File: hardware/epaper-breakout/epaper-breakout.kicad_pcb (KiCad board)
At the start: 2 copper layers, 100 x 40.5 mm, 101 parts, among them J1 XF2M-3315-1A, J2 C10418, J3 Conn_02x05_Counter_Clockwise, J4 ED060SC4, J5 Conn_01x01_Male, J6 Conn_01x01_Male, J7 Conn_01x12, Q1 AO3401A, Q3 MMBT3904, Q4 MMBT3904, U1 MCP1700-3302E_SOT23, U11 TP4056, U12 CH340C, U2 PCA9555PW, U3 TPS651851RSLR, U4 XC6206PxxxMR, U5 ESP32-WROVER, U6 ED060XC5

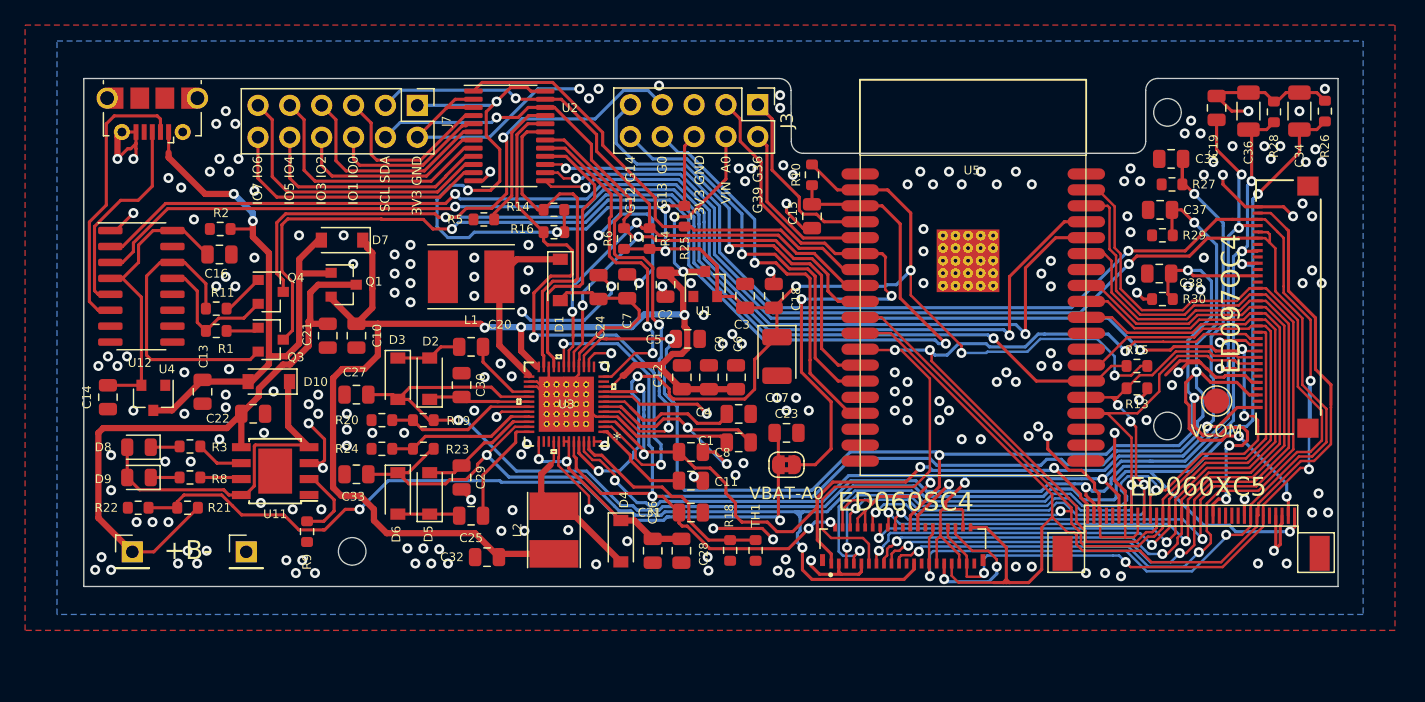
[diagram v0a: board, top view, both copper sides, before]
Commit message: add additional ground area
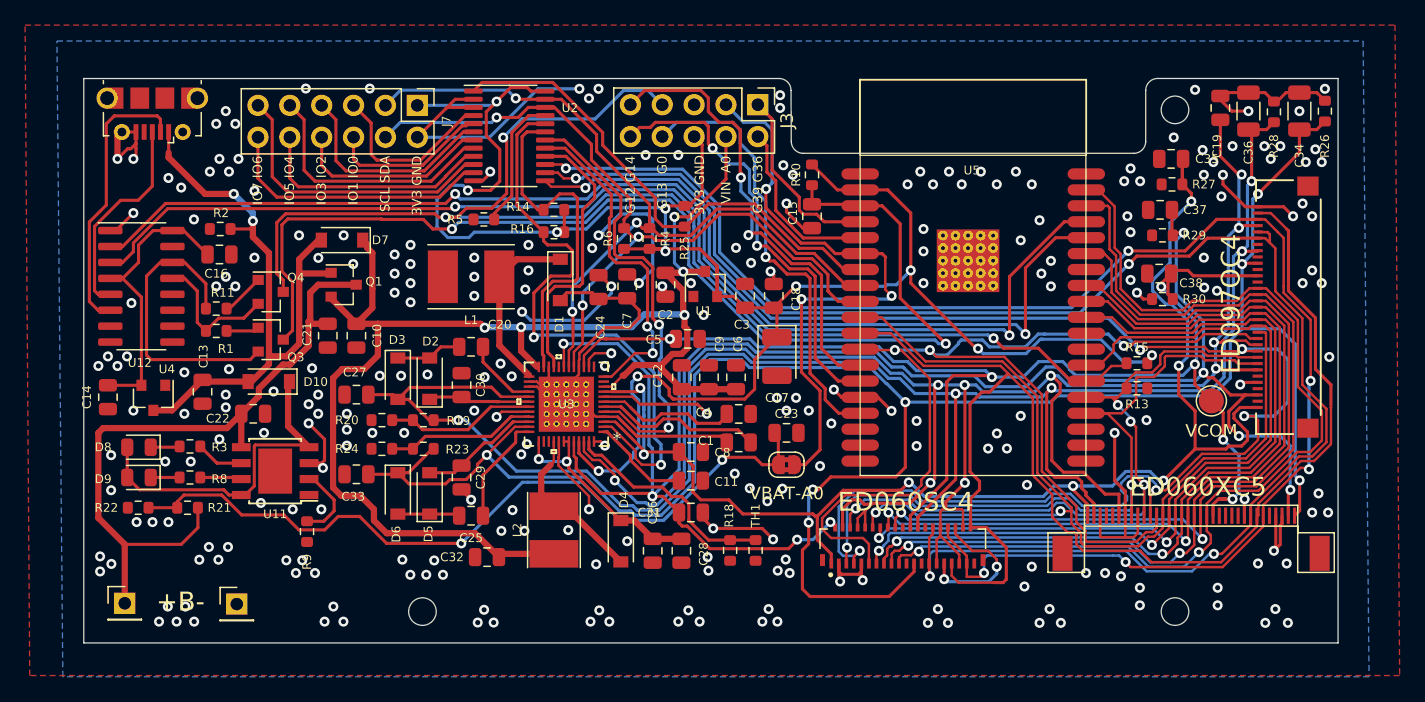
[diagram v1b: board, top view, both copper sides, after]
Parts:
- moved H3 14.8 mm to (112.0, 62.0)
- moved H2 7.38 mm to (52.0, 62.0)
- moved J6 4.23 mm to (37.2, 61.4)
- moved J5 4.14 mm to (28.3, 61.3)
- moved H1 0.63 mm to (112.0, 22.0)
- moved TP_VCOM1 0.42 mm to (114.9, 45.2)
- moved C19 0.30 mm to (115.6, 21.8)
- moved R15 0.22 mm to (109.0, 42.2)
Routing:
- net EPD_VDD: track 127.4 -> 155.2 mm, vias 8 -> 10
- net /+22V: track 147.0 -> 169.3 mm, vias 5 -> 7
- net /-20V: track 124.2 -> 144.9 mm
- net GND: track 198.8 -> 178.7 mm, vias 231 -> 261
- net /EP_VCOM: track 115.5 -> 104.3 mm
- net /EP_CKV: track 93.4 -> 102.9 mm
- net /EP_OE: track 122.5 -> 128.7 mm
- net BAT+: track 49.8 -> 54.9 mm
- net /EP_STV: track 131.1 -> 126.6 mm
- net /MOSI: track 31.4 -> 35.6 mm
- net /EP_D0: track 72.8 -> 76.3 mm
- net /MISO: track 32.1 -> 35.2 mm, vias 1 -> 2
- net /EP_STH: track 90.3 -> 92.8 mm
- net /SCL: track 61.3 -> 63.1 mm
- net /SDA: track 61.4 -> 63.1 mm
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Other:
- board size 100 x 40.5 mm -> 100 x 45 mm

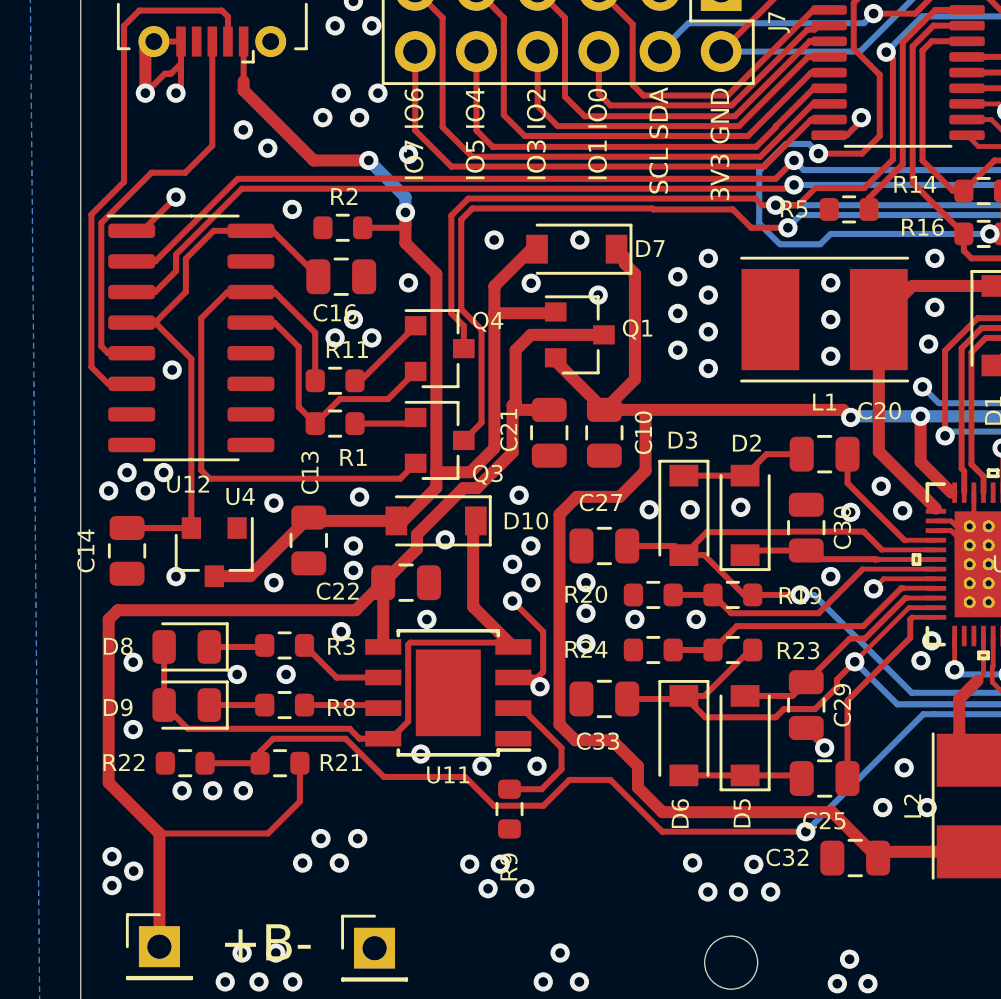
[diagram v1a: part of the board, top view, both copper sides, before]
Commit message: add tps2113 for power switchover
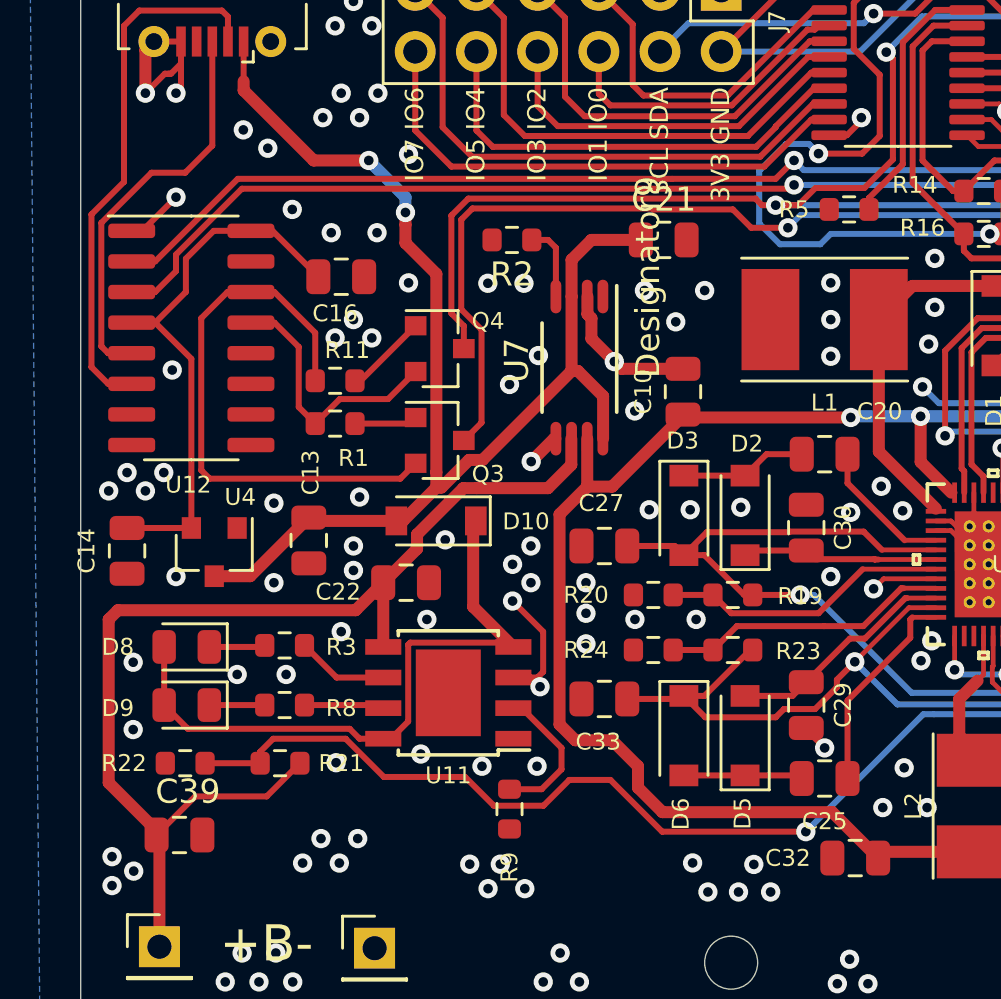
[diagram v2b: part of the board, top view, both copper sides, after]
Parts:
- removed D7: 1N5817, Diode_SMD:D_SOD-123
- removed Q1: AO3401A, Package_TO_SOT_SMD:SOT-23
- added C39: 0.1uF, Capacitor_SMD:C_0805_2012Metric, F.Cu at (29.1, 56.7)
- added U7: , epaper-breakout:TPS2113APW, F.Cu at (45.7, 37.3)
- C21: value 10uF -> 0.1uF
- R2: value 100k -> 400
- moved C21 9.31 mm to (49.2, 32.0), turned to 0 degrees
- moved R2 7.04 mm to (42.9, 32.0), turned to 180 degrees
- moved C10 3.68 mm to (50.0, 38.3), turned to 270 degrees
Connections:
- C21 pad 1: BAT+ -> VBUS
- R2 pad 1: GND -> Net-(R2-Pad1)
- R2 pad 2: VBUS -> GND
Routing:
- net SW_VIN: track 126.0 -> 114.0 mm
- net GND: track 178.7 -> 186.6 mm, vias 261 -> 259
- net BAT+: track 54.9 -> 47.6 mm
- net Net-(R2-Pad1): track 0.00 -> 3.16 mm
- net VBUS: track 50.4 -> 53.0 mm
